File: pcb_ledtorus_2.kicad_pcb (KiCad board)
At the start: 4 copper layers, 200 x 200 mm, 273 parts, among them P1 CONN_02X04, P2 CONN_6, P3 MICRO-SD, P4 CONN_2, P5 KNUSB, P6 CONN_12, U1 STM32F46X_LQFP176, U10 TLC5955, U11 TLC5955, U12 TLC5955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

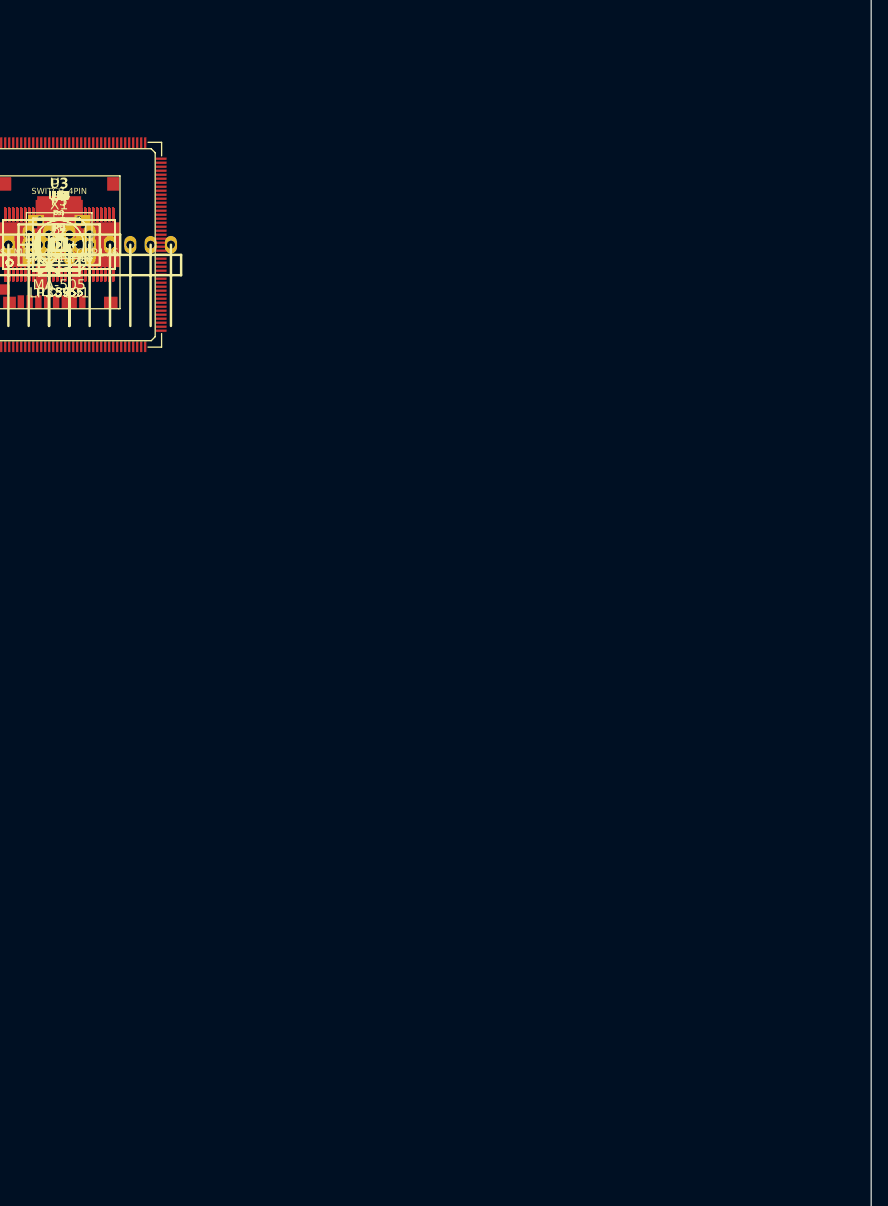
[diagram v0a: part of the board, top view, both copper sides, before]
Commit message: Place LEDs for PCB routing.
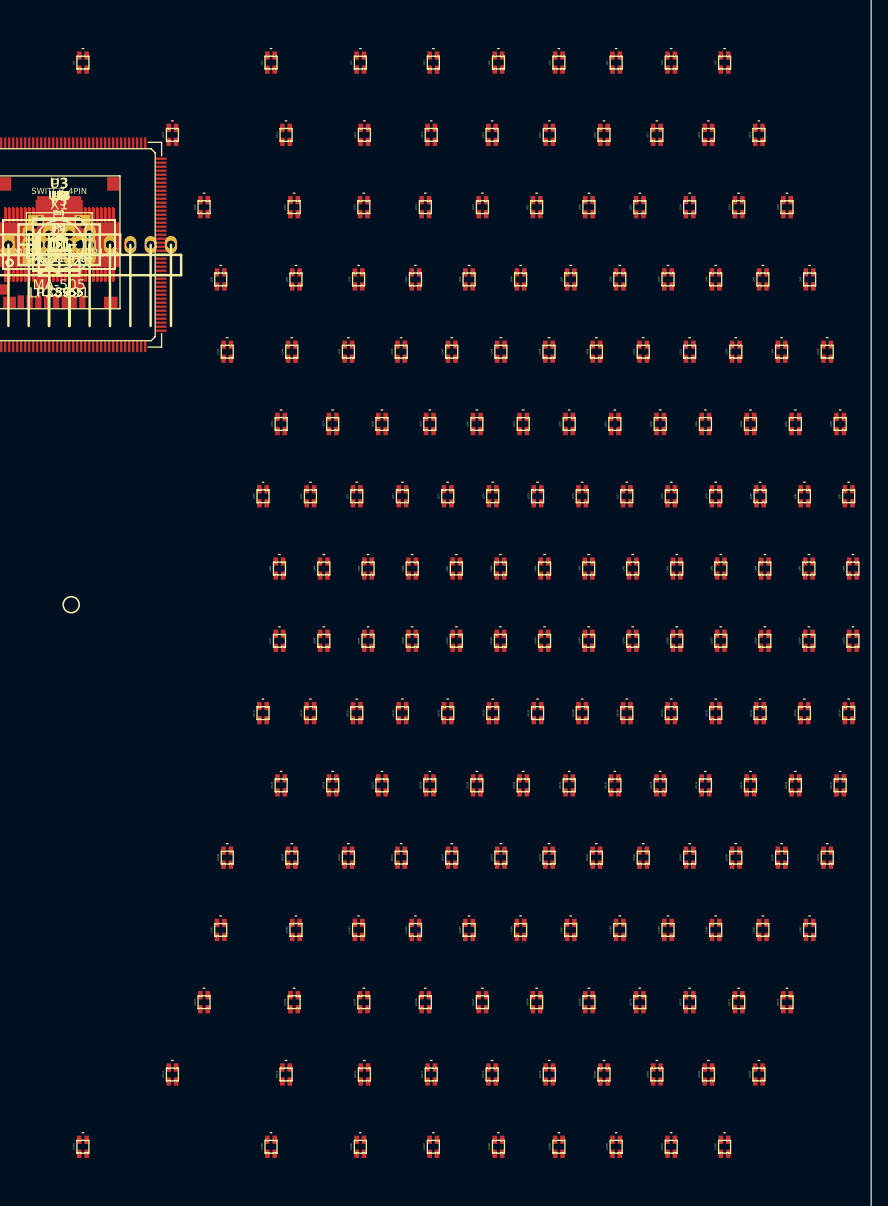
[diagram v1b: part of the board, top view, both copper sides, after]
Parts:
- moved LD192 140.1 mm to (231.7, 217.8), turned to 90 degrees
- moved LD191 136.3 mm to (225.0, 217.8), turned to 90 degrees
- moved LD183 135.7 mm to (236.0, 208.7), turned to 90 degrees
- moved LD190 132.5 mm to (218.1, 217.8), turned to 90 degrees
- moved LD182 131.7 mm to (229.7, 208.7), turned to 90 degrees
- moved LD173 131.3 mm to (239.5, 199.7), turned to 90 degrees
- moved LD189 128.9 mm to (211.0, 217.8), turned to 90 degrees
- moved LD181 127.8 mm to (223.2, 208.7), turned to 90 degrees
- moved LD172 127.2 mm to (233.4, 199.7), turned to 90 degrees
- moved LD162 127.0 mm to (242.3, 190.7), turned to 90 degrees
- moved LD188 125.4 mm to (203.4, 217.8), turned to 90 degrees
- moved LD180 124.1 mm to (216.6, 208.7), turned to 90 degrees
- moved LD171 123.2 mm to (227.3, 199.7), turned to 90 degrees
- moved LD150 122.8 mm to (244.5, 181.6), turned to 90 degrees
- moved LD161 122.8 mm to (236.5, 190.7), turned to 90 degrees
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
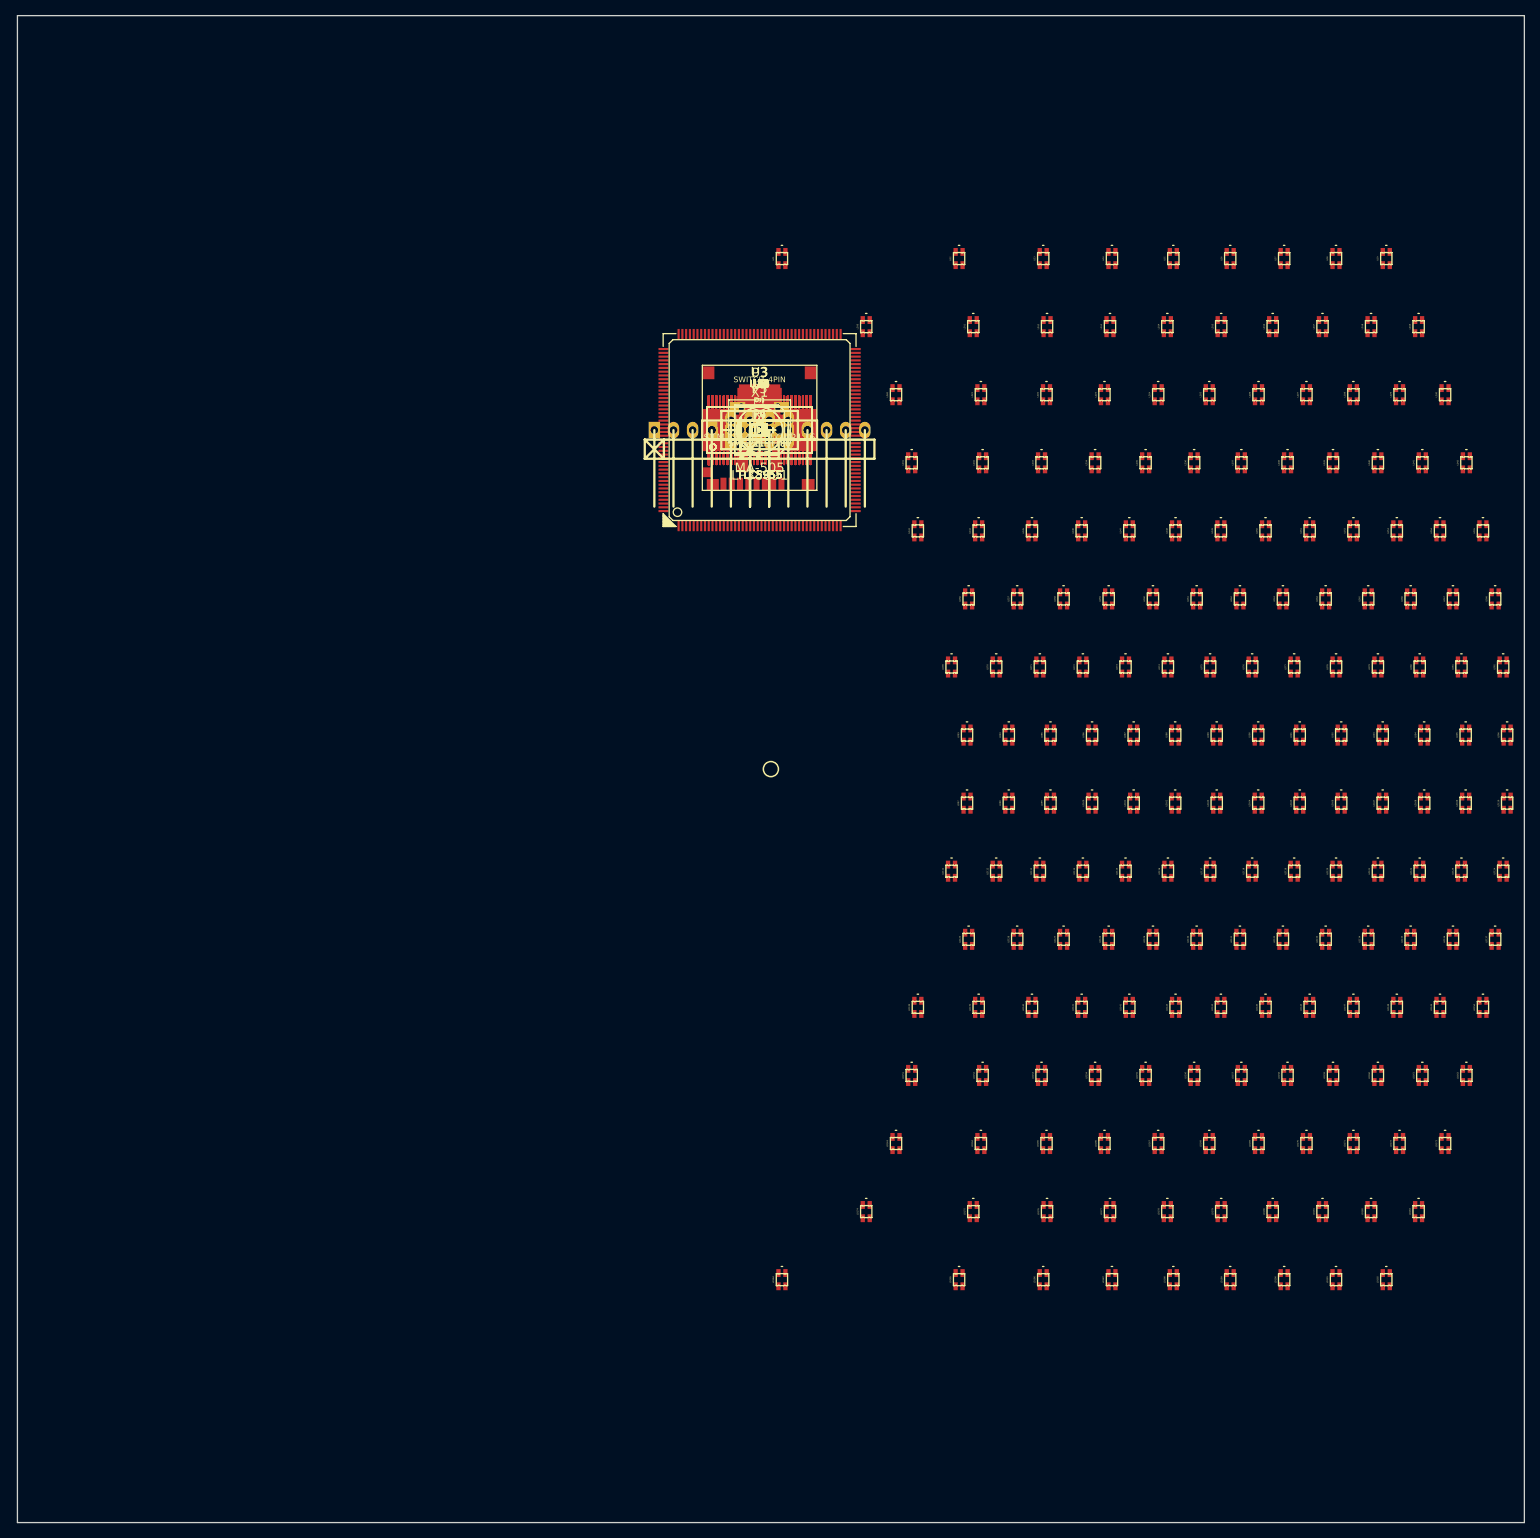
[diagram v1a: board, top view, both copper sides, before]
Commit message: Add elliptical board outline
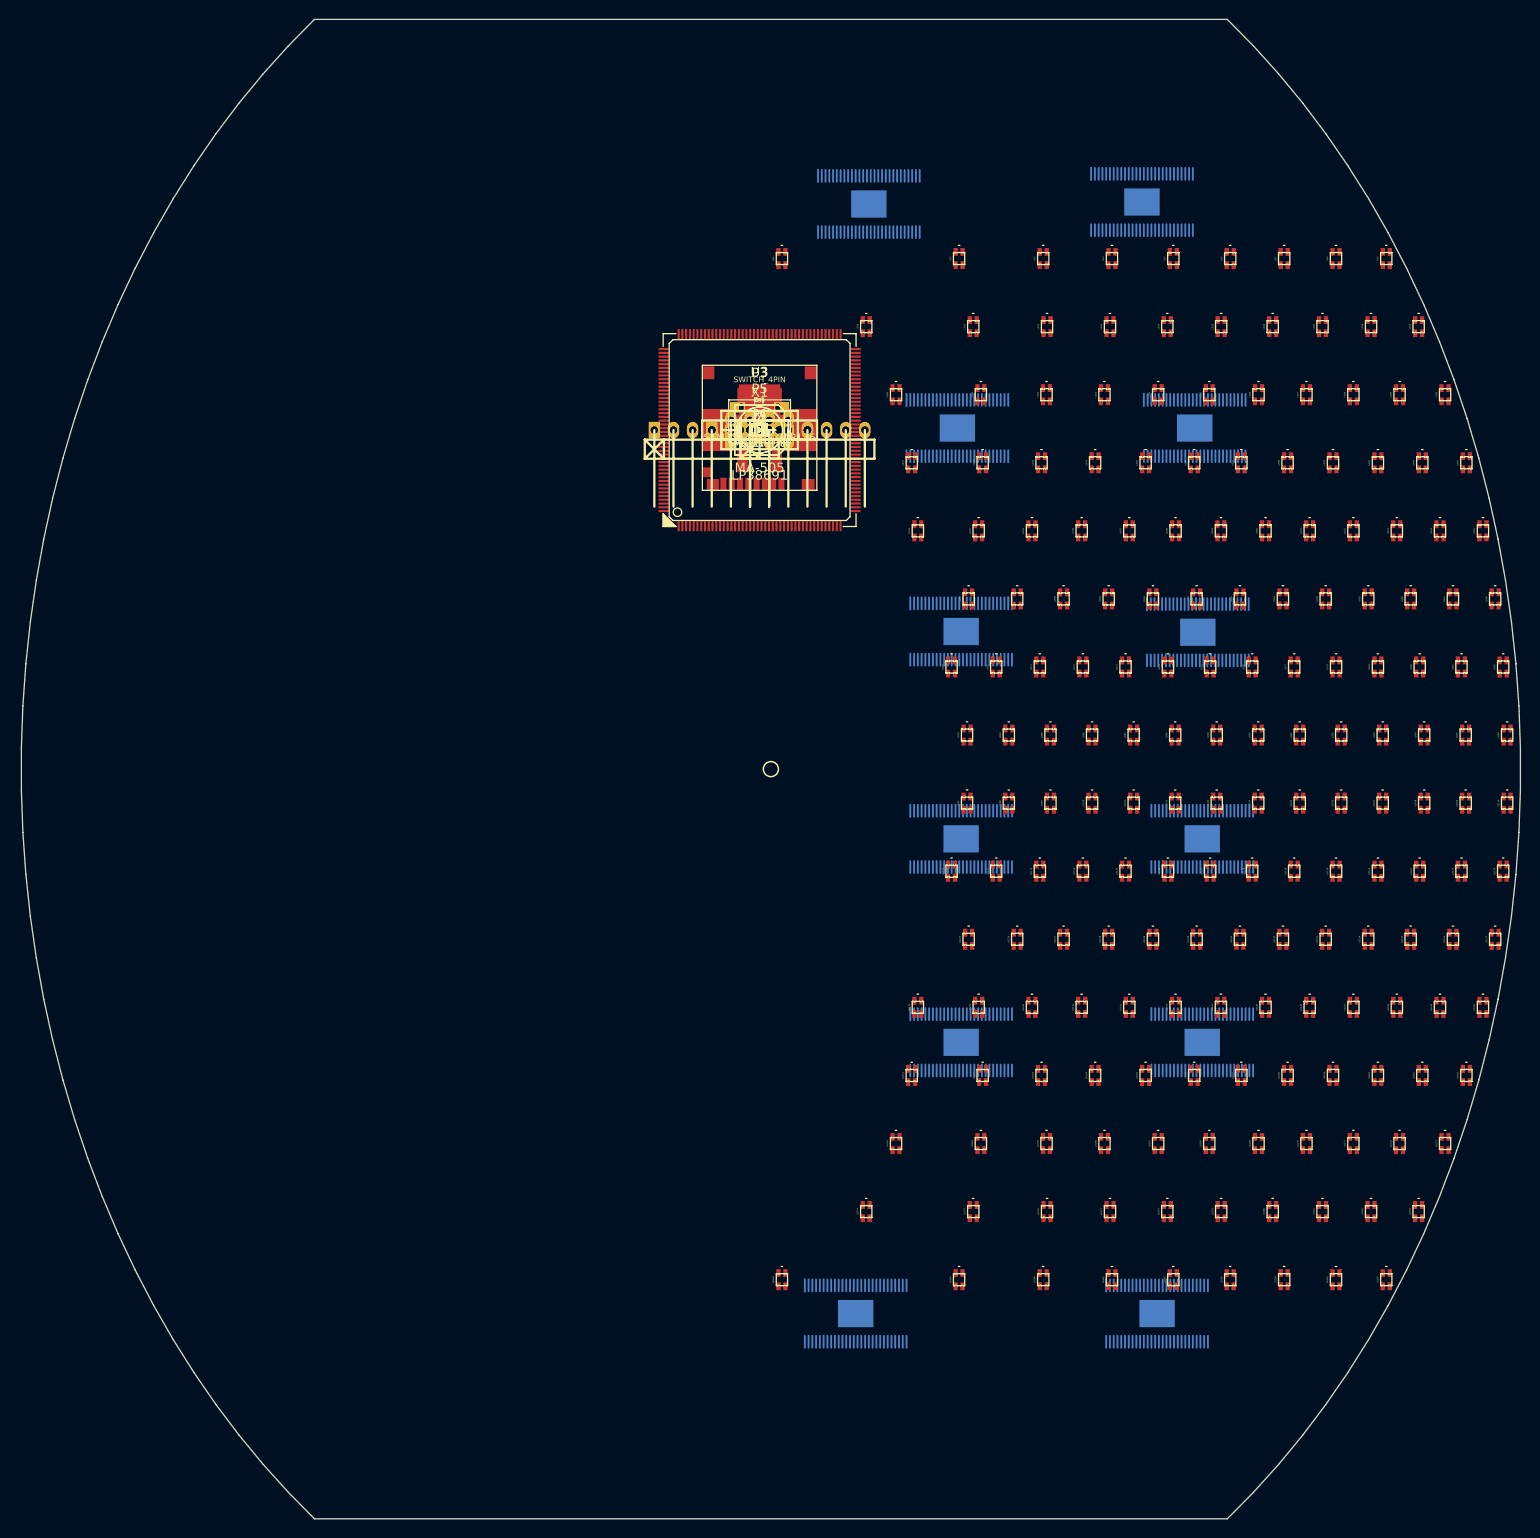
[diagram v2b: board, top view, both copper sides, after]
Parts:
- U10, U11, U12, U13, U14, U15, U4, U5, U6, U7, U8, U9: moved to B.Cu
- moved U15 128.6 mm to (201.2, 222.3)
- moved U14 117.9 mm to (161.2, 222.3)
- moved U13 100.3 mm to (207.2, 186.3)
- moved U12 85.5 mm to (175.2, 186.3)
- moved U11 80.0 mm to (207.2, 159.3)
- moved U9 64.1 mm to (206.7, 131.8)
- moved U10 60.5 mm to (175.2, 159.3)
- moved U5 59.1 mm to (199.2, 74.7)
- moved U7 57.7 mm to (206.2, 104.7)
- moved U8 37.8 mm to (175.2, 131.7)
- moved U4 33.3 mm to (163.0, 75.0)
- moved U6 26.3 mm to (174.8, 104.7)
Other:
- board size 200 x 200 mm -> 199 x 199 mm

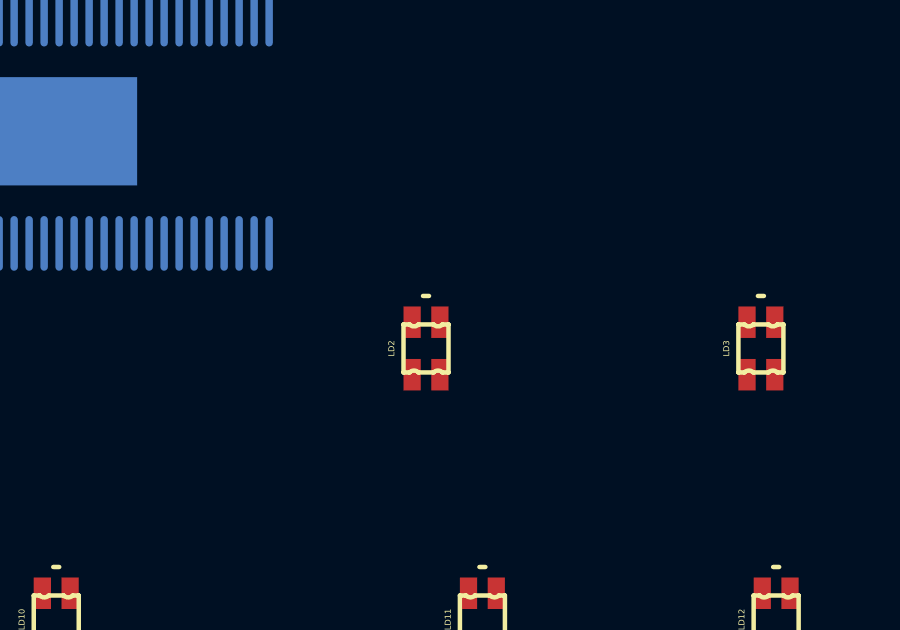
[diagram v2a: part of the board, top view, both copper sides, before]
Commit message: Add power planes
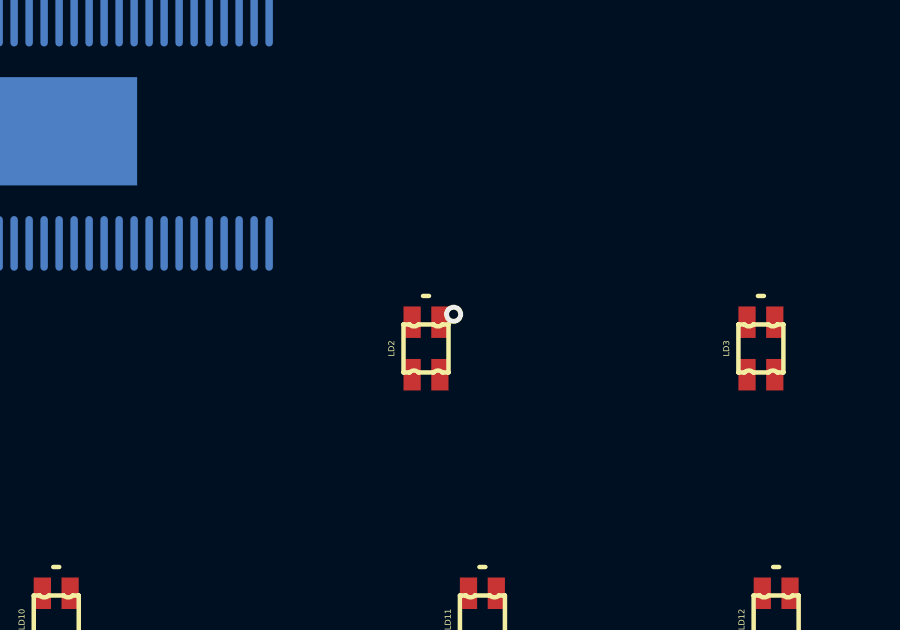
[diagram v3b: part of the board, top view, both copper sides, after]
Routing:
- net +5V: track 0.00 -> 0.57 mm, vias 0 -> 1
- added copper zone on In1.Cu, net +5V
- added copper zone on In2.Cu, net GND
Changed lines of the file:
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@@
   (general
     (links 1069)
-    (no_connects 911)
-    (area 49.924999 49.924999 250.075001 250.075001)
+    (no_connects 973)
+    (area 50 50 250.000001 250.000001)
     (thickness 0.8)
-    (drawings 23)
-    (tracks 0)
+    (drawings 85)
+    (tracks 3)
     (zones 0)
     (modules 273)
@@
     (user_trace_width 1.016)
     (trace_clearance 0.2032)
-    (zone_clearance 0.508)
+    (zone_clearance 0.2032)
     (zone_45_only no)
     (trace_min 0.1524)
@@
       (net 11 /Power/osc_out))
   )
-  (gr_line (start 214.038448 54.010849) (end 210.571762 50.500000) (layer Edge.Cuts) (width 0.15))
+  (gr_line (start 214.038448 54.010849) (end 210.571762 50.5) (layer Edge.Cuts) (width 0.15))
   (gr_line (start 217.377214 57.713438) (end 214.038448 54.010849) (layer Edge.Cuts) (width 0.15))
   (gr_line (start 220.581393 61.600373) (end 217.377214 57.713438) (layer Edge.Cuts) (width 0.15))
@@
   (gr_line (start 217.377214 242.286562) (end 220.581393 238.399627) (layer Edge.Cuts) (width 0.15))
   (gr_line (start 214.038448 245.989151) (end 217.377214 242.286562) (layer Edge.Cuts) (width 0.15))
-  (gr_line (start 210.571762 249.500000) (end 214.038448 245.989151) (layer Edge.Cuts) (width 0.15))
-  (gr_line (start 89.428238 249.500000) (end 210.571762 249.500000) (layer Edge.Cuts) (width 0.15))
-  (gr_line (start 85.961552 245.989151) (end 89.428238 249.500000) (layer Edge.Cuts) (width 0.15))
+  (gr_line (start 210.571762 249.5) (end 214.038448 245.989151) (layer Edge.Cuts) (width 0.15))
+  (gr_line (start 89.428238 249.5) (end 210.571762 249.5) (layer Edge.Cuts) (width 0.15))
+  (gr_line (start 85.961552 245.989151) (end 89.428238 249.5) (layer Edge.Cuts) (width 0.15))
   (gr_line (start 82.622786 242.286562) (end 85.961552 245.989151) (layer Edge.Cuts) (width 0.15))
   (gr_line (start 79.418607 238.399627) (end 82.622786 242.286562) (layer Edge.Cuts) (width 0.15))
@@
   (gr_line (start 82.622786 57.713438) (end 79.418607 61.600373) (layer Edge.Cuts) (width 0.15))
   (gr_line (start 85.961552 54.010849) (end 82.622786 57.713438) (layer Edge.Cuts) (width 0.15))
-  (gr_line (start 89.428238 50.500000) (end 85.961552 54.010849) (layer Edge.Cuts) (width 0.15))
-  (gr_line (start 210.571762 50.500000) (end 89.428238 50.500000) (layer Edge.Cuts) (width 0.15))
+  (gr_line (start 89.428238 50.5) (end 85.961552 54.010849) (layer Edge.Cuts) (width 0.15))
+  (gr_line (start 210.571762 50.5) (end 89.428238 50.5) (layer Edge.Cuts) (width 0.15))
   (gr_circle (center 150 150) (end 151 150) (layer F.SilkS) (width 0.2))
+  (segment (start 175.441676 81.364465) (end 175.635535 81.364465) (width 0.2032) (layer F.Cu) (net 6) (status C00000))
+  (segment (start 175.635535 81.364465) (end 175.9 81.1) (width 0.2032) (layer F.Cu) (net 6) (status 400000))
+  (via (at 175.9 81.1) (size 0.635) (drill 0.3048) (layers F.Cu B.Cu) (net 6))
+  (zone (net 2) (net_name GND) (layer In2.Cu) (hatch edge 0.508)
+    (connect_pads (clearance 0.2032))
+    (min_thickness 0.2032)
+    (fill yes (arc_segments 16) (thermal_gap 0.2032) (thermal_bridge_width 0.508))
+    (polygon
+      (pts
+        (xy 250 250) (xy 50 250) (xy 50 50) (xy 250 50) (xy 250 250)
+      )
+    )
+  )
+  (zone (net 6) (net_name +5V) (layer In1.Cu) (hatch edge 0.508)
+    (connect_pads (clearance 0.2032))
+    (min_thickness 0.2032)
+    (fill yes (arc_segments 16) (thermal_gap 0.2032) (thermal_bridge_width 0.508))
+    (polygon
+      (pts
+        (xy 250 250) (xy 150 250) (xy 150 50) (xy 250 50) (xy 250 250)
+      )
+    )
+  )
 )
